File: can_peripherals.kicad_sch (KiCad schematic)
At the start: 14 parts, among them U4 MCP2515, U5 MCP2551, Y1 ABLS7M-16.000MHZ-B-2-T

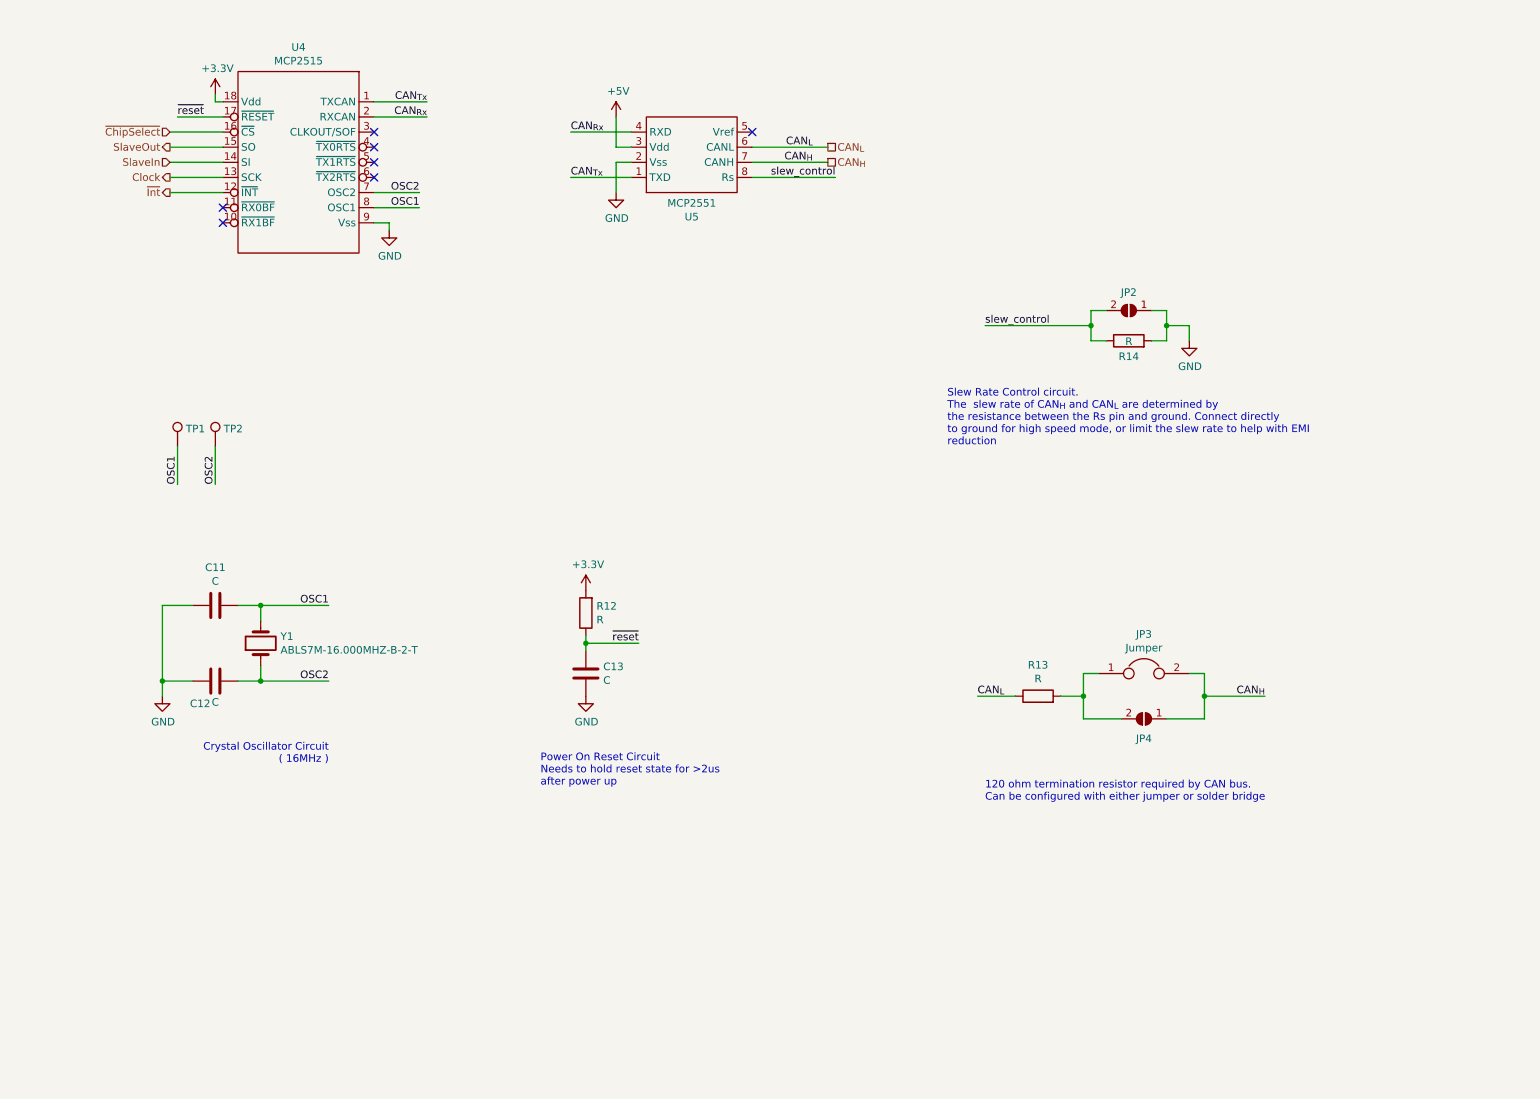
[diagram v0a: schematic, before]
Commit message: Routing for HDMI, Ethernet, SD Card, CAN
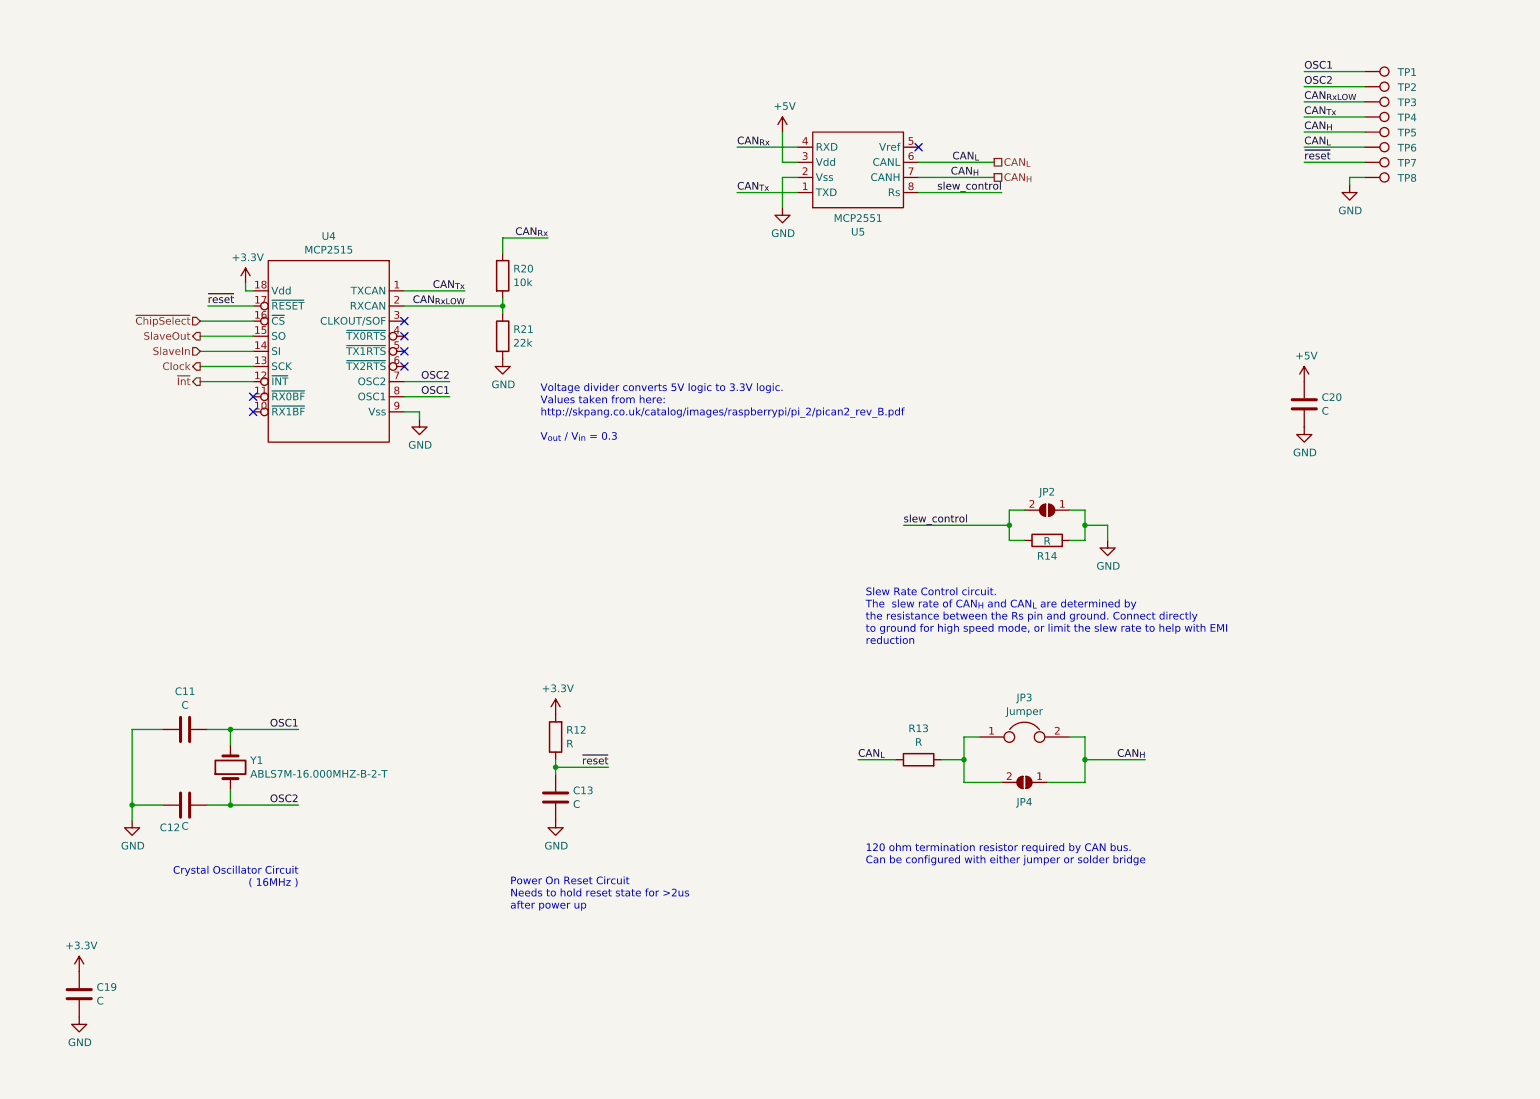
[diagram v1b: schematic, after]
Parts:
- added C19, C20: C, Capacitor_SMD:C_0805_2012Metric, symbol Device:C
- added R20: 10k, Resistor_SMD:R_0805_2012Metric, symbol Device:R
- added R21: 22k, Resistor_SMD:R_0805_2012Metric, symbol Device:R
- added TP3, TP4, TP5, TP6, TP7, TP8: TestPoint, TestPoint:TestPoint_Pad_D1.5mm, symbol Connector:TestPoint
- Y1: footprint (none) -> footprints:Crystal-ABLS7M
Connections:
- net +3V3: now also C19.1
- net +5V: now also C20.1
- net CAN_{H}: now also TP5.1
- net CAN_{L}: now also TP6.1
- net CAN_{Rx}: now also R20.1; no longer U4.2 (RXCAN)
- net CAN_{Tx}: now also TP4.1
- net GND: now also C19.2, C20.2, R21.2, TP8.1
- net ~reset: now also TP7.1
- new net CAN_{RxLOW}: R20.2, R21.1, TP3.1, U4.2 (RXCAN)
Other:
- note added: "Voltage divider converts 5V logic to 3.3V logic. Values taken from here: http://skpang.co.uk/catalog/images/raspberrypi/pi_2/pican2_rev_B.pdf V_{out} / V_{in} = 0.3"
- moved on the sheet: C11, C12, C13, JP2, JP3, JP4, R12, R13, R14, TP1, TP2, U4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

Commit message: Finished trace routing
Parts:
- R21: renamed from R20; value 10k -> R
- R22: renamed from R21; value 22k -> R
- renumbered C19 to C18, C11 to C19, C12 to C20, C13 to C21, C20 to C22, JP2 to JP5, R12 to R23, R13 to R24, R14 to R25, TP2 to TP10, TP3 to TP11, TP4 to TP12, TP5 to TP13, TP6 to TP14, TP7 to TP15, TP8 to TP16, TP1 to TP9, U4 to U5, U5 to U6, Y1 to Y2

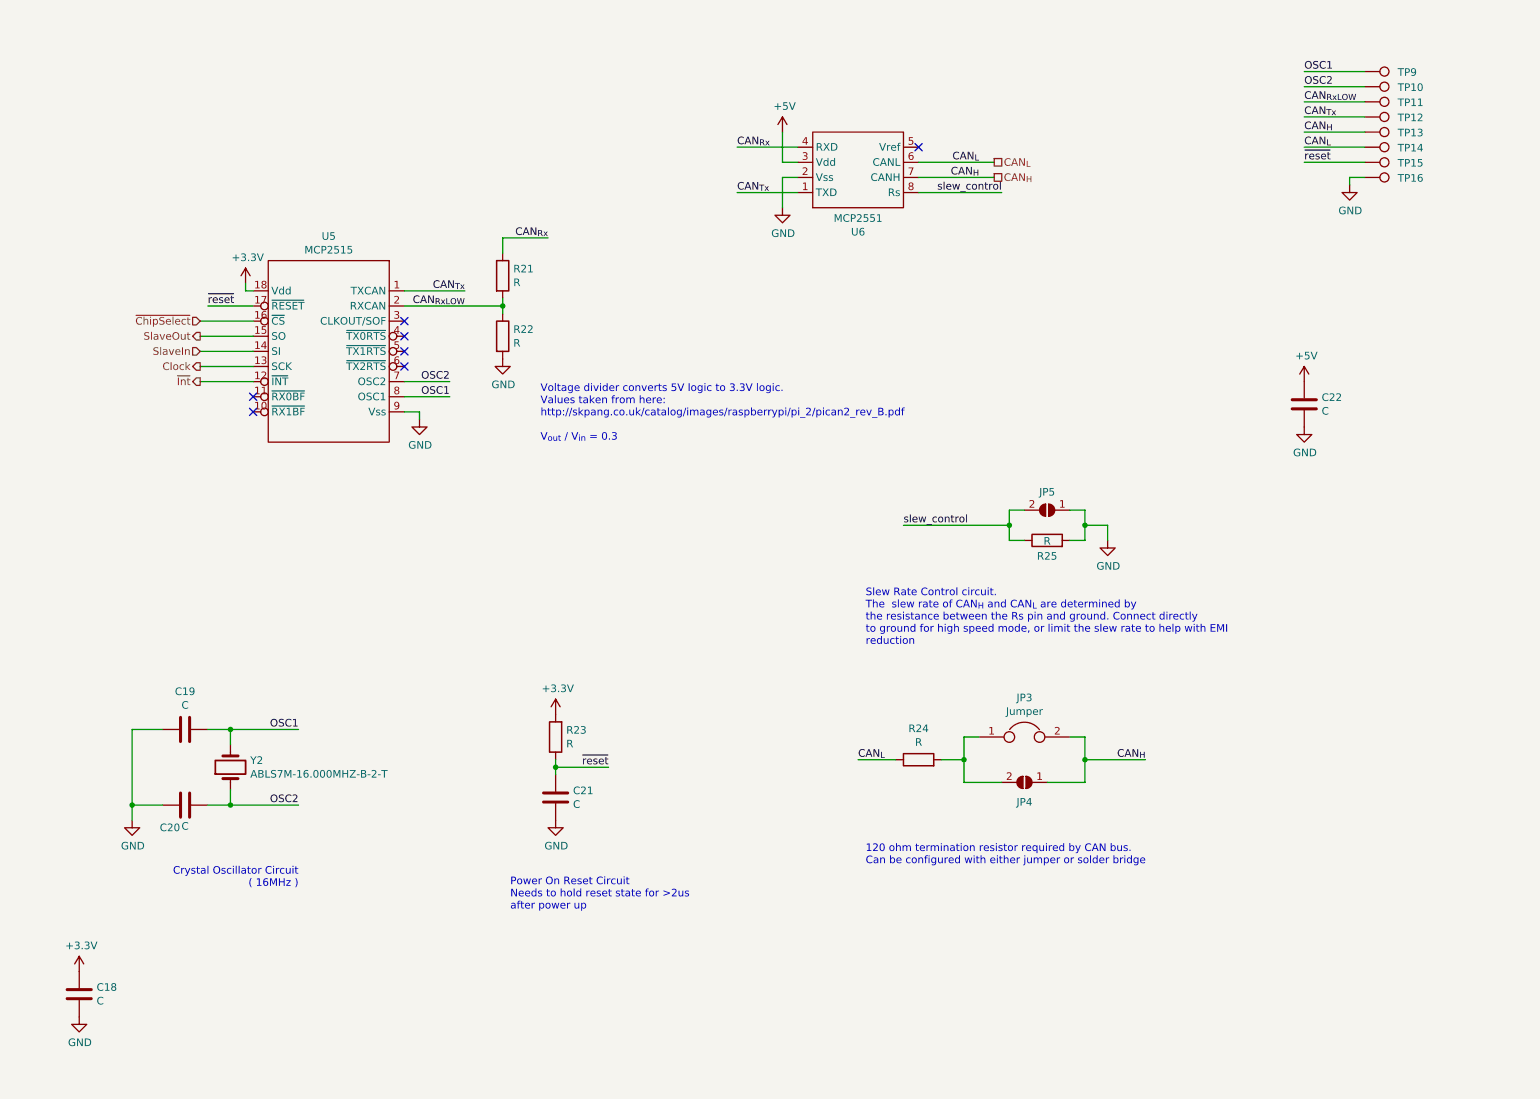
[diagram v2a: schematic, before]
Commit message: Cleaning up
Reassigned reference designators to better match their position on the board.
Moved USB hub IC and related circuits to their own sheet in the schematic.
Tweaked reference designator positions on board to improve visibility.
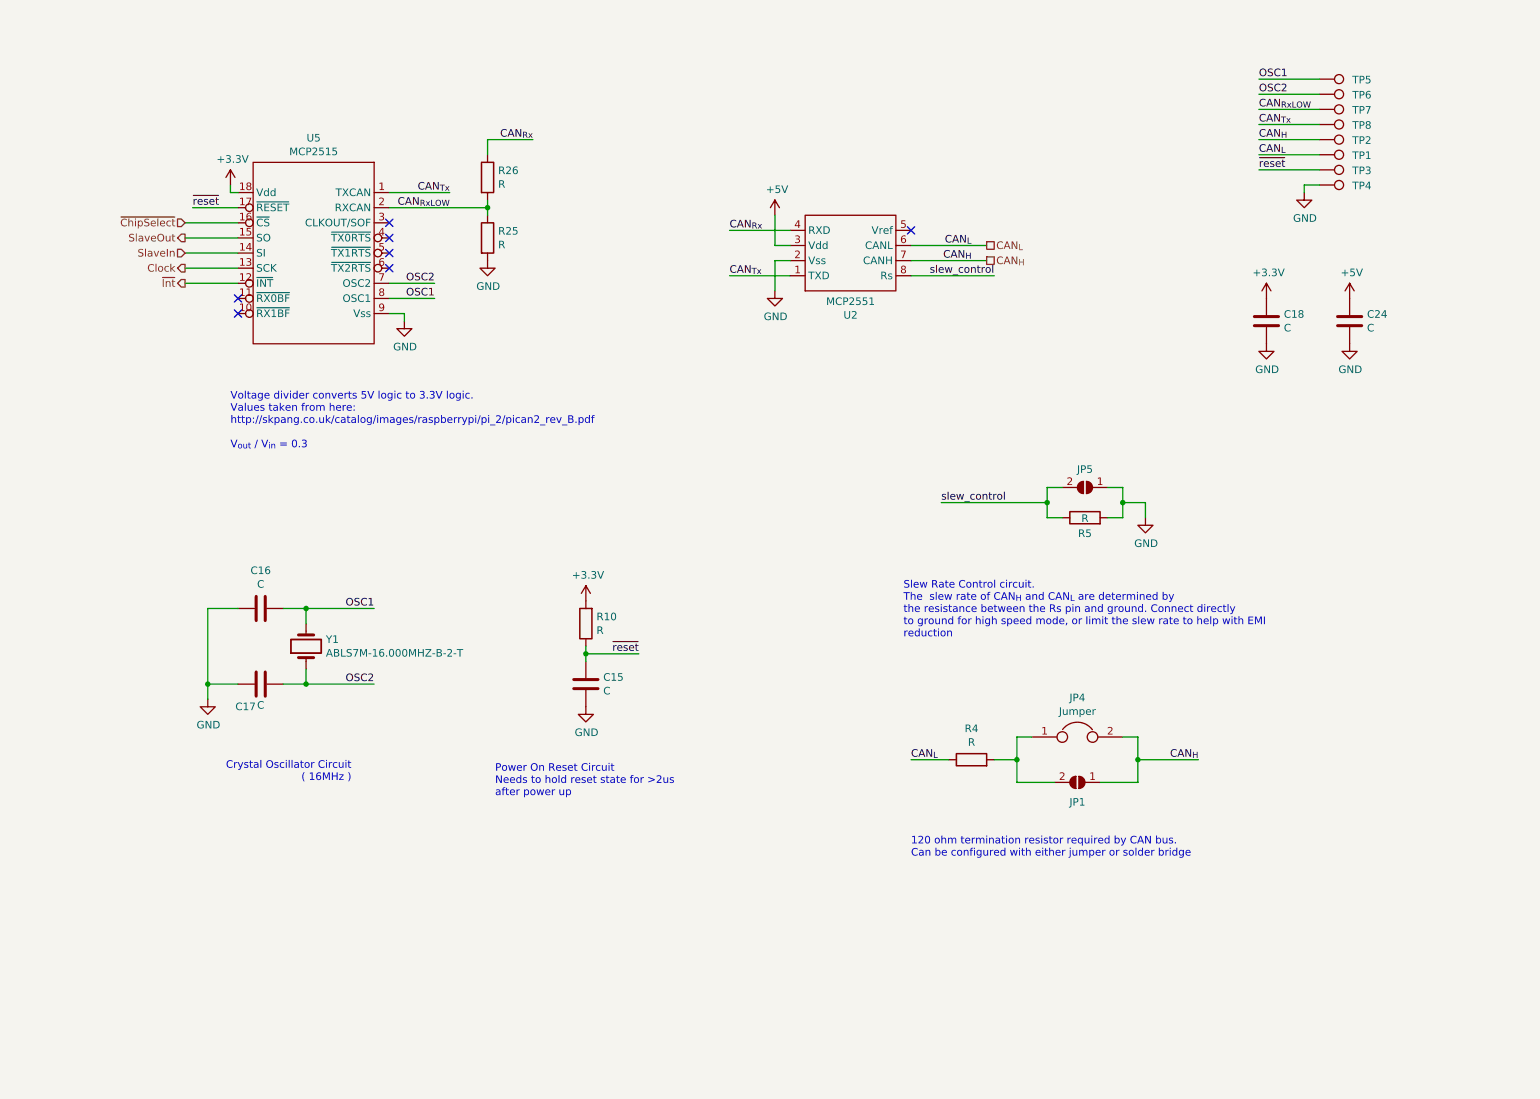
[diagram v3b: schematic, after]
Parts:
- renumbered C21 to C15, C19 to C16, C20 to C17, C22 to C24, JP4 to JP1, JP3 to JP4, R23 to R10, R22 to R25, R21 to R26, R24 to R4, R25 to R5, TP14 to TP1, TP13 to TP2, TP15 to TP3, TP16 to TP4, TP9 to TP5, TP10 to TP6, TP11 to TP7, TP12 to TP8, U6 to U2, Y2 to Y1
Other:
- moved on the sheet: C15, C16, C17, C18, C24, JP1, JP4, JP5, R10, R25, R26, R4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

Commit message: migrated computers
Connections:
- net ~ChipSelect renamed ~{ChipSelect}
- net ~Int renamed ~{Int}
- net ~reset renamed ~{reset}
